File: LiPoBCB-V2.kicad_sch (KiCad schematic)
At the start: 11 parts

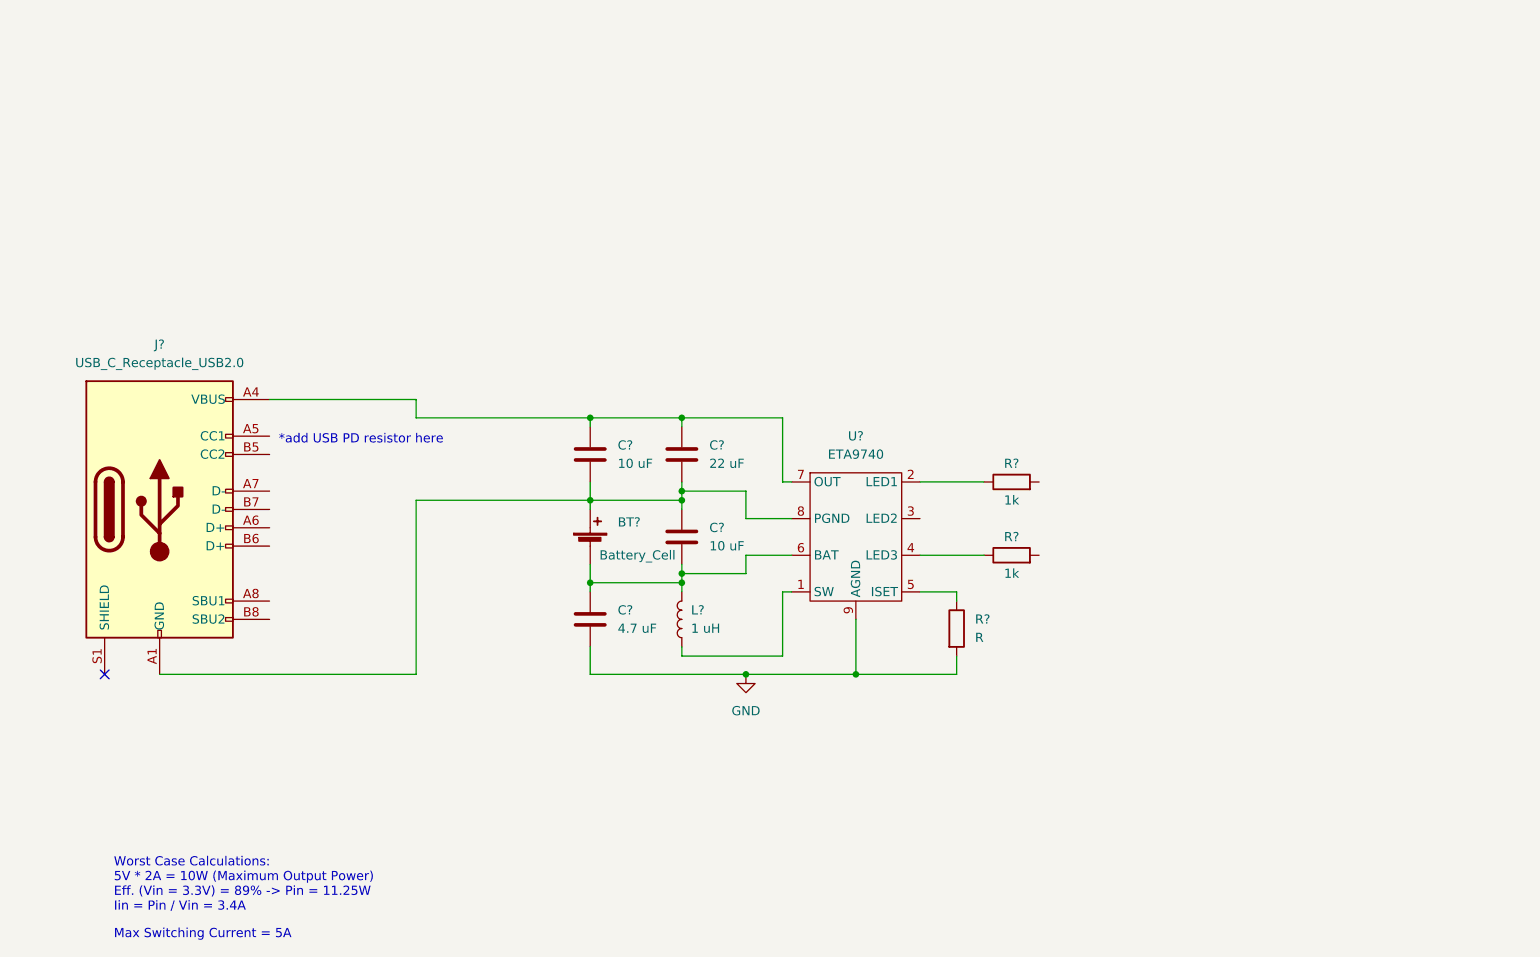
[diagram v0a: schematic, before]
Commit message: added usb-c port
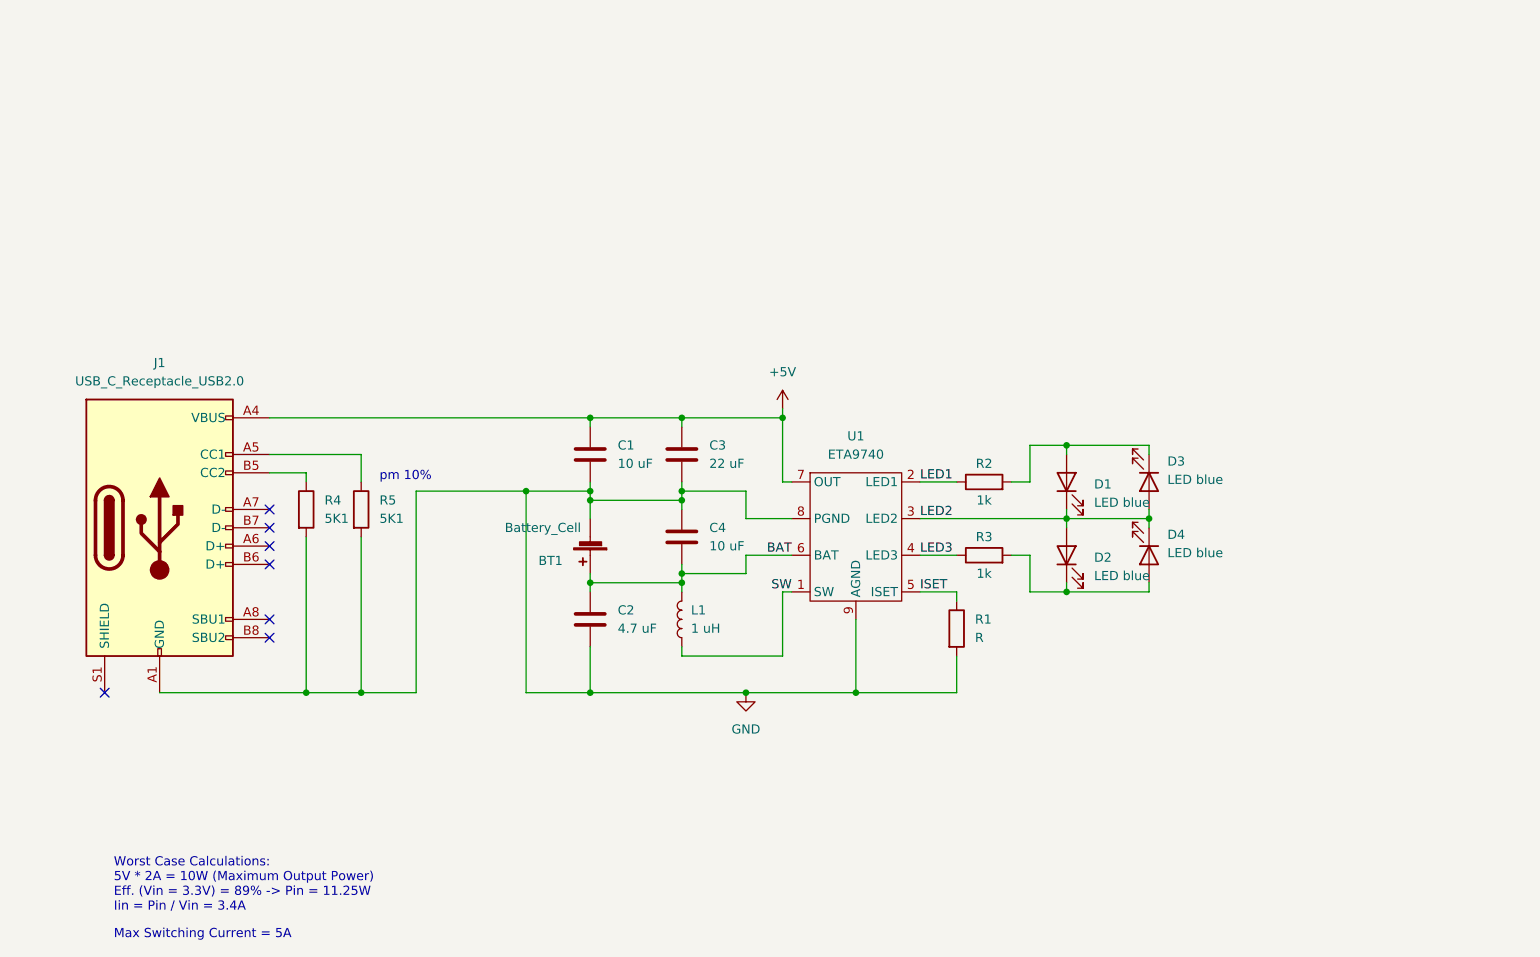
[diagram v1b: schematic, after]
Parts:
- added D1, D2, D3, D4: LED blue, Diode_SMD:D_0603_1608Metric, symbol Device:LED
- added R4, R5: 5K1, Resistor_SMD:R_0603_1608Metric, symbol Device:R
- C1, C2, C4: renamed from C?; footprint (none) -> Capacitor_SMD:C_0603_1608Metric
- C3: renamed from C?; footprint (none) -> Capacitor_SMD:C_0805_2012Metric
- L1: renamed from L?; footprint (none) -> LiPoBCB-V2:L_smd_1616
- R1: renamed from R?; footprint (none) -> Resistor_SMD:R_0603_1608Metric_Pad0.98x0.95mm_HandSolder
- R2, R3: renamed from R?; footprint (none) -> Resistor_SMD:R_0603_1608Metric
- gave numbers to parts that had none: 3
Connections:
- net GND: now also BT1.2 (-), C1.2, C3.2, C4.1, J1.A1 (GND), J1.A12 (GND), J1.B1 (GND), J1.B12 (GND), U1.8 (PGND), R4.2, R5.2
- net +5V: now reaches C1.1, C3.1, J1.A4 (VBUS), J1.A9 (VBUS), J1.B4 (VBUS), J1.B9 (VBUS), U1.7 (OUT)
- net at J1.A5 (CC1): now also R5.1
- net at J1.B5 (CC2): now also R4.1
- net BAT: now reaches C2.1, C4.2, L1.2, U1.6 (BAT)
- net BAT: now also BT1.1 (+); no longer BT1.2 (-)
- net ISET: now reaches R1.1, U1.5 (ISET)
- net SW: now reaches L1.1, U1.1 (SW)
- net LED1: now reaches R2.1, U1.2 (LED1)
- net LED2: now reaches U1.3 (LED2)
- net LED2: now also D1.1 (K), D2.2 (A), D3.2 (A), D4.1 (K)
- net LED3: now reaches R3.1, U1.4 (LED3)
- net at R2.2: now also D1.2 (A), D3.1 (K)
- net at R3.2: now also D2.1 (K), D4.2 (A)
- no-connect marks 1 -> 7
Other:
- note added: "pm 10%"
- note removed: "*add USB PD resistor here"
- moved on the sheet: BT1, J1, R2, R3

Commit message: added fets
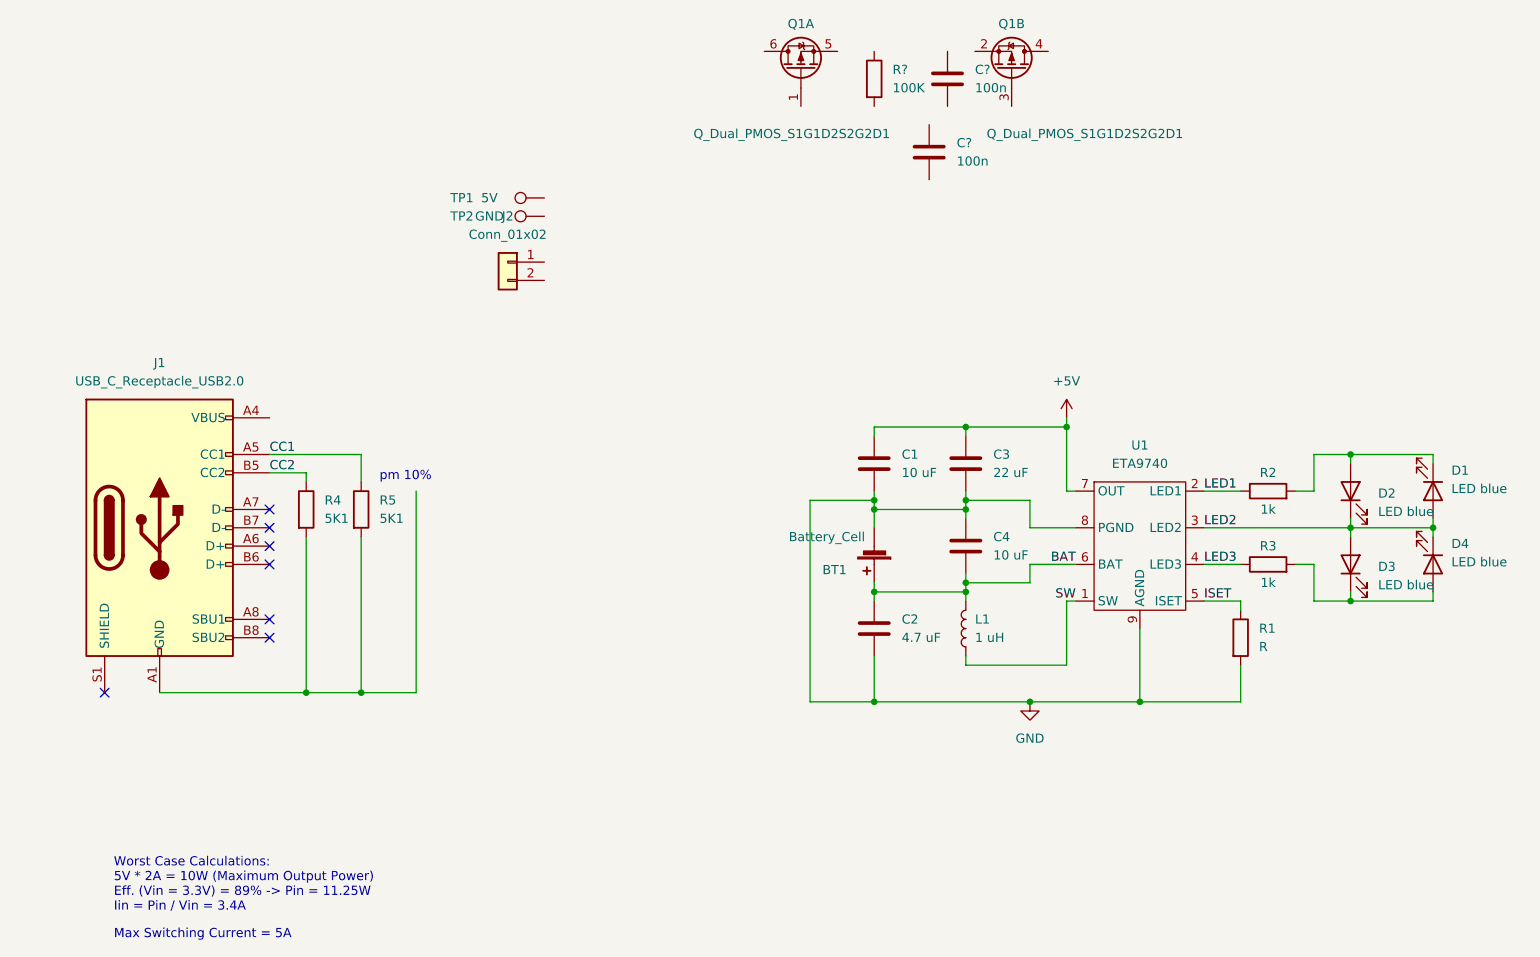
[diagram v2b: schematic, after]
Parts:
- added C? (x2): 100n, Capacitor_SMD:C_0603_1608Metric, symbol Device:C
- added J2: Conn_01x02, symbol Connector_Generic:Conn_01x02
- added Q1: Q_Dual_PMOS_S1G1D2S2G2D1, Package_TO_SOT_SMD:SOT-23-6, symbol Device:Q_Dual_PMOS_S1G1D2S2G2D1
- added R?: 100K, Resistor_SMD:R_0603_1608Metric, symbol Device:R
- added TP1: 5V, TestPoint:TestPoint_THTPad_2.5x2.5mm_Drill1.2mm, symbol Connector:TestPoint
- added TP2: GND, TestPoint:TestPoint_THTPad_2.5x2.5mm_Drill1.2mm, symbol Connector:TestPoint
- BT1: footprint (none) -> Connector_JST:JST_PH_B2B-PH-K_1x02_P2.00mm_Vertical
- J1: footprint (none) -> LiPoBCB-V2:Korean Hroparts Elec TYPE-C-31-M-17
- renumbered D3 to D1, D1 to D2, D2 to D3
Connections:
- net +5V: no longer J1.A4 (VBUS), J1.A9 (VBUS), J1.B4 (VBUS), J1.B9 (VBUS)
- net GND: no longer J1.A1 (GND), J1.A12 (GND), J1.B1 (GND), J1.B12 (GND), R4.2, R5.2
- net CC1: now reaches J1.A5 (CC1), R5.1
- net CC2: now reaches J1.B5 (CC2), R4.1
- new net: J1.A1 (GND), J1.A12 (GND), J1.B1 (GND), J1.B12 (GND), R4.2, R5.2
- new net: J1.A4 (VBUS), J1.A9 (VBUS), J1.B4 (VBUS), J1.B9 (VBUS)
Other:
- moved on the sheet: BT1, C1, C2, C3, C4, D1, D2, D3, D4, L1, R1, R2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

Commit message: replaced usb-c port
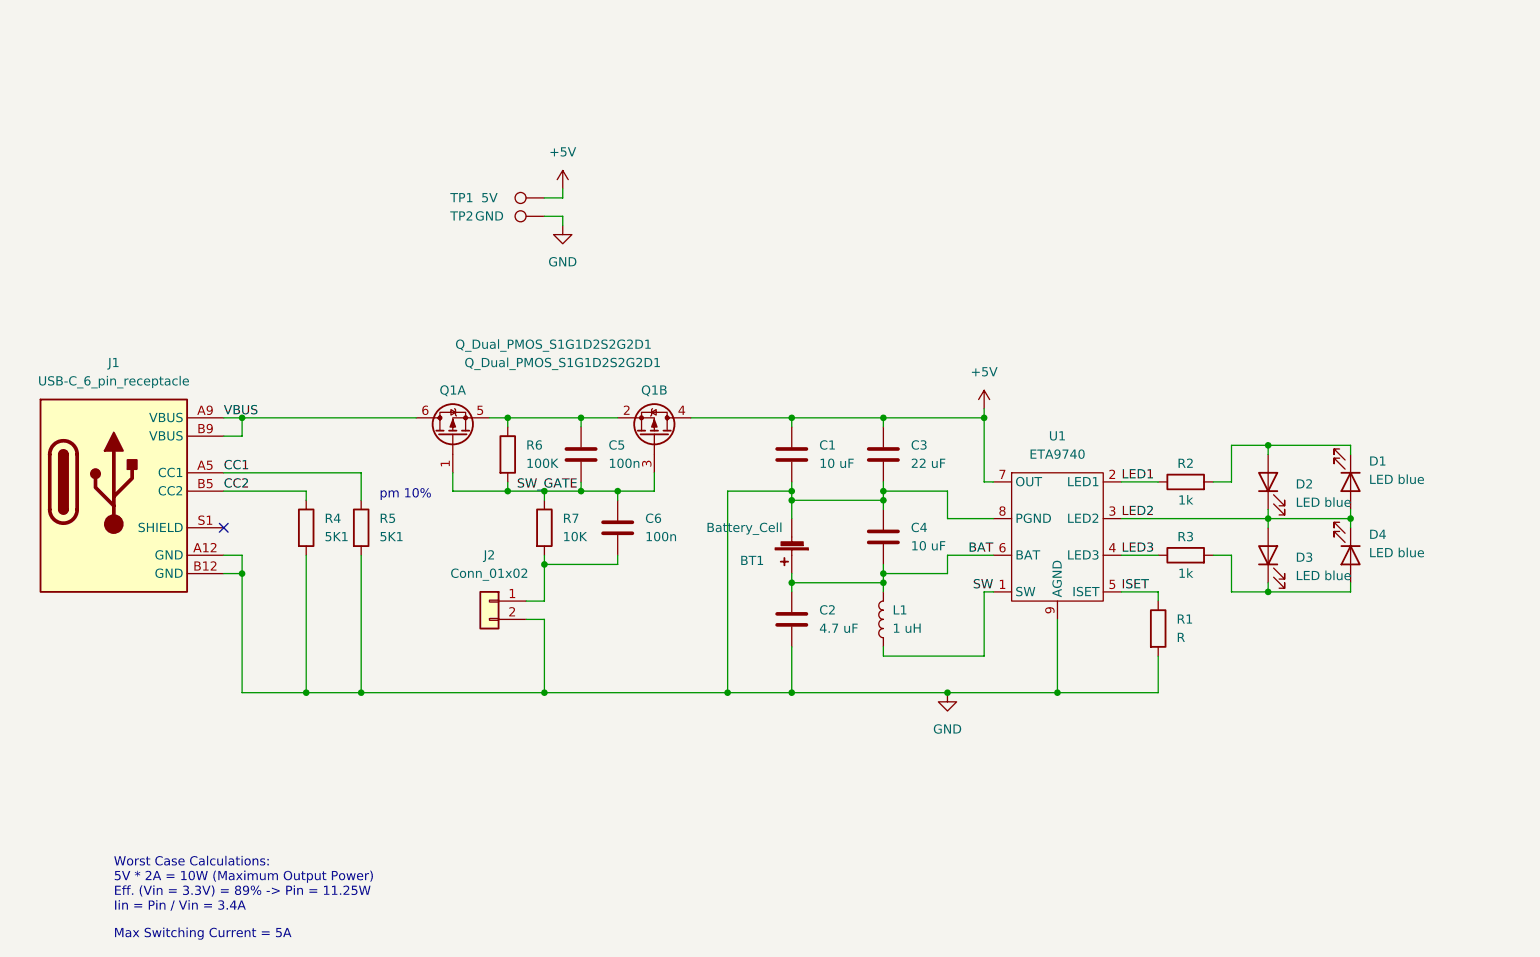
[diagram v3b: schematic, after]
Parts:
- removed J1: USB_C_Receptacle_USB2.0, LiPoBCB-V2:Korean Hroparts Elec TYPE-C-31-M-17, symbol Connector:USB_C_Receptacle_USB2.0
- added J1: USB-C_6_pin_receptacle, LiPoBCB-V2:Korean Hroparts Elec TYPE-C-31-M-17, symbol LiPoBCB-V2:USB-C_6_pin_receptacle
- added R7: 10K, Resistor_SMD:R_0603_1608Metric, symbol Device:R
- D1, D2, D3, D4: footprint Diode_SMD:D_0603_1608Metric -> LiPoBCB-V2:D_0603_1608Metric
- J2: footprint (none) -> Connector_PinHeader_2.54mm:PinHeader_1x02_P2.54mm_Vertical
- gave numbers to parts that had none: 3
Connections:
- net +5V: now also Q1.4 (D), TP1.1
- net CC1: now also J1.A5 (CC1)
- net CC2: now also J1.B5 (CC2)
- net GND: now also J2.2 (Pin_2), R4.2, R5.2, TP2.1, J1.A12 (GND), J1.B12 (GND)
- net SW_GATE: now reaches C6.1
- net SW_GATE: now also C5.2, Q1.1 (G), Q1.3 (G), R6.2, R7.1
- net at C6.2: now also J2.1 (Pin_1), R7.2
- net at C5.1: now also Q1.2 (S), Q1.5 (S), R6.1
- net VBUS: now reaches Q1.6 (D)
- net VBUS: now also J1.A9 (VBUS), J1.B9 (VBUS)
- no-connect marks 7 -> 1
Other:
- moved on the sheet: BT1, C1, C2, C3, C4, C5, C6, D1, D2, D3, D4, J2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

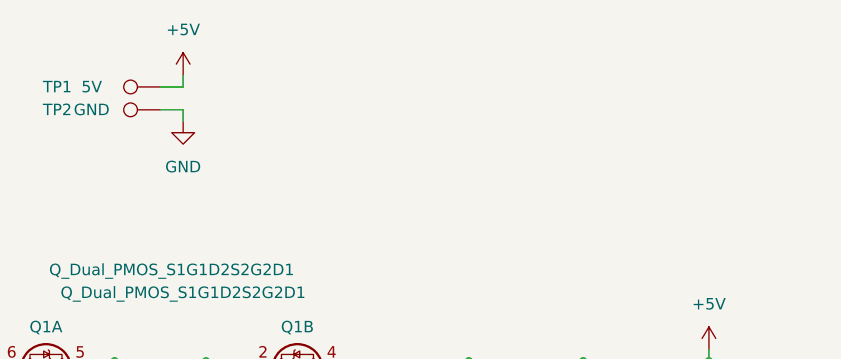
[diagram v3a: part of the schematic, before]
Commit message: created board outline
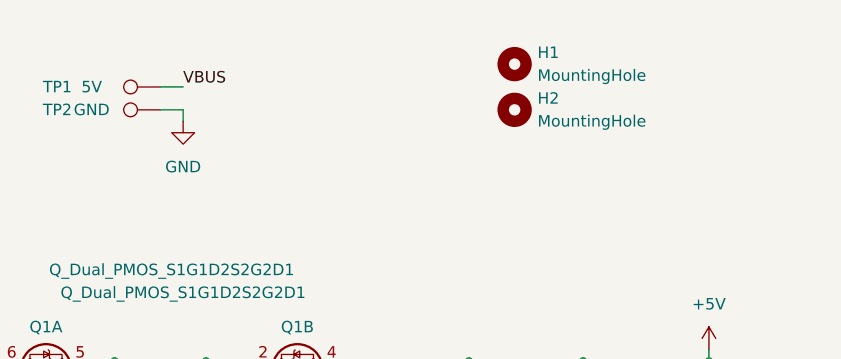
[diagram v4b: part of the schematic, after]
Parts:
- added H1, H2: MountingHole, MountingHole:MountingHole_2.2mm_M2_ISO14580, symbol Mechanical:MountingHole
- R1: footprint Resistor_SMD:R_0603_1608Metric_Pad0.98x0.95mm_HandSolder -> Resistor_SMD:R_0603_1608Metric
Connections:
- net +5V: no longer TP1.1
- net VBUS: now also TP1.1
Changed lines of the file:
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@@
-    (stroke (width 0) (type default) (color 0 0 0 0))
-  )
-  (wire (pts (xy 104.14 54.61) (xy 104.14 53.34))
     (stroke (width 0) (type default) (color 0 0 0 0))
   )
@@
   (label "SW" (at 163.83 109.22 180)
     (effects (font (size 1.27 1.27)) (justify right bottom))
+  )
+  (label "VBUS" (at 104.14 54.61 0)
+    (effects (font (size 1.27 1.27)) (justify left bottom))
   )
   (label "LED2" (at 181.61 99.06 0)
@@
       (effects (font (size 1.27 1.27)) (justify left))
     )
-    (property "Footprint" "Resistor_SMD:R_0603_1608Metric_Pad0.98x0.95mm_HandSolder" (id 2) (at 184.912 114.3 90)
+    (property "Footprint" "Resistor_SMD:R_0603_1608Metric" (id 2) (at 184.912 114.3 90)
       (effects (font (size 1.27 1.27)) hide)
     )
@@
     (pin "1")
     (pin "2")
-  )
-  (symbol (lib_id "power:+5V") (at 104.14 53.34 0) (unit 1)
-    (in_bom yes) (on_board yes) (fields_autoplaced)
-    (property "Reference" "#PWR0104" (id 0) (at 104.14 57.15 0)
-      (effects (font (size 1.27 1.27)) hide)
-    )
-    (property "Value" "+5V" (id 1) (at 104.14 48.26 0))
-    (property "Footprint" "" (id 2) (at 104.14 53.34 0)
-      (effects (font (size 1.27 1.27)) hide)
-    )
-    (property "Datasheet" "" (id 3) (at 104.14 53.34 0)
-      (effects (font (size 1.27 1.27)) hide)
-    )
-    (pin "1")
   )
   (symbol (lib_id "Device:C") (at 148.59 101.6 0) (unit 1)
@@
     (pin "3")
     (pin "4")
+  )
+  (symbol (lib_id "Mechanical:MountingHole") (at 140.97 57.15 0) (unit 1)
+    (in_bom yes) (on_board yes) (fields_autoplaced)
+    (property "Reference" "H2" (id 0) (at 143.51 55.8799 0)
+      (effects (font (size 1.27 1.27)) (justify left))
+    )
+    (property "Value" "MountingHole" (id 1) (at 143.51 58.4199 0)
+      (effects (font (size 1.27 1.27)) (justify left))
+    )
+    (property "Footprint" "MountingHole:MountingHole_2.2mm_M2_ISO14580" (id 2) (at 140.97 57.15 0)
+      (effects (font (size 1.27 1.27)) hide)
+    )
+    (property "Datasheet" "~" (id 3) (at 140.97 57.15 0)
+      (effects (font (size 1.27 1.27)) hide)
+    )
   )
   (symbol (lib_id "Device:L") (at 148.59 113.03 180) (unit 1)
@@
     (pin "S1")
   )
+  (symbol (lib_id "Mechanical:MountingHole") (at 140.97 52.07 0) (unit 1)
+    (in_bom yes) (on_board yes) (fields_autoplaced)
+    (property "Reference" "H1" (id 0) (at 143.51 50.7999 0)
+      (effects (font (size 1.27 1.27)) (justify left))
+    )
+    (property "Value" "MountingHole" (id 1) (at 143.51 53.3399 0)
+      (effects (font (size 1.27 1.27)) (justify left))
+    )
+    (property "Footprint" "MountingHole:MountingHole_2.2mm_M2_ISO14580" (id 2) (at 140.97 52.07 0)
+      (effects (font (size 1.27 1.27)) hide)
+    )
+    (property "Datasheet" "~" (id 3) (at 140.97 52.07 0)
+      (effects (font (size 1.27 1.27)) hide)
+    )
+  )
   (symbol (lib_id "Device:LED") (at 213.36 93.98 270) (unit 1)
     (in_bom yes) (on_board yes)
@@
       (reference "#PWR0103") (unit 1) (value "GND") (footprint "")
     )
-    (path "/39131da6-4ddc-4367-86d2-f04f4f13df84"
-      (reference "#PWR0104") (unit 1) (value "+5V") (footprint "")
-    )
     (path "/cd64ba69-008d-430c-814f-55bd818560d0"
       (reference "BT1") (unit 1) (value "Battery_Cell") (footprint "Connector_JST:JST_PH_B2B-PH-K_1x02_P2.00mm_Vertical")
@@
       (reference "D4") (unit 1) (value "LED blue") (footprint "LiPoBCB-V2:D_0603_1608Metric")
     )
+    (path "/bc334cae-df70-4615-b4c4-e2015e128c82"
+      (reference "H1") (unit 1) (value "MountingHole") (footprint "MountingHole:MountingHole_2.2mm_M2_ISO14580")
+    )
+    (path "/71cb5197-ce2a-42ae-b7be-22433559aaa8"
+      (reference "H2") (unit 1) (value "MountingHole") (footprint "MountingHole:MountingHole_2.2mm_M2_ISO14580")
+    )
     (path "/ba88f274-0232-4d0f-aeb6-b970e2e9c1ee"
       (reference "J1") (unit 1) (value "USB-C_6_pin_receptacle") (footprint "LiPoBCB-V2:Korean Hroparts Elec TYPE-C-31-M-17")
@@
     )
     (path "/2f82e466-af26-4f9e-bab5-60f4195fd7ea"
-      (reference "R1") (unit 1) (value "R") (footprint "Resistor_SMD:R_0603_1608Metric_Pad0.98x0.95mm_HandSolder")
+      (reference "R1") (unit 1) (value "R") (footprint "Resistor_SMD:R_0603_1608Metric")
     )
     (path "/b4eb8eaa-de54-4175-9925-6b835fc3905f"
